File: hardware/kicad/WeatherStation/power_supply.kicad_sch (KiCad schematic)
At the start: 20 parts, among them J1 USB-C (GCT USB4105), J2 Solar 6V (JST-PH), J3 18650 LiPo (JST-PH), U2 TP4056, U2A DW01A, U3 AMS1117-3.3

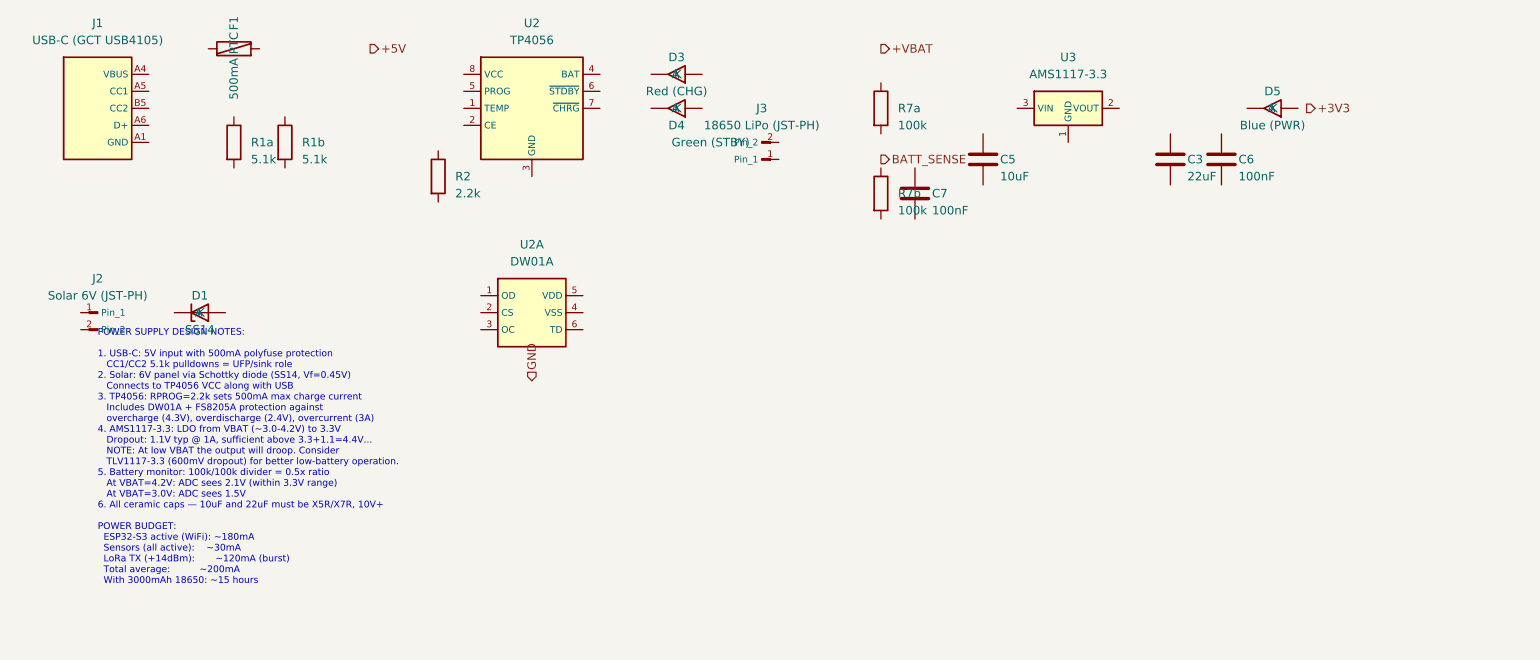
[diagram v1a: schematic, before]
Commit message: Fix 4: power_supply.kicad_sch — fix AMS1117 cap note, add VBAT cap, fix battery label, update power budget
Agent-Logs-Url: https://github.com/ppusapati/weather/sessions/bf78e071-0670-4802-a032-1f4282b37237

Co-authored-by: ppusapati <5749576+ppusapati@users.noreply.github.com>
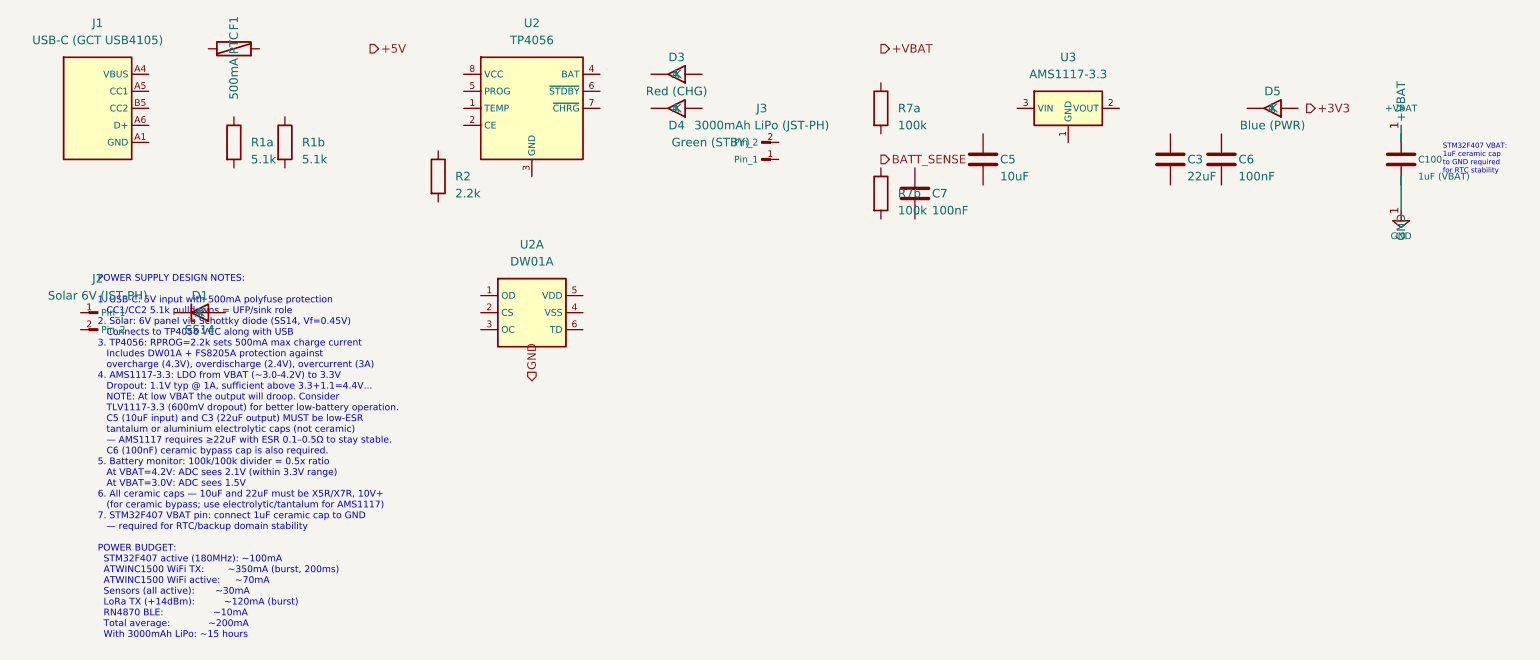
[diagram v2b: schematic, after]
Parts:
- added C100: 1uF (VBAT), symbol Device:C
- J3: value 18650 LiPo (JST-PH) -> 3000mAh LiPo (JST-PH)
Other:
- note added: "STM32F407 VBAT: 1uF ceramic cap to GND required for RTC stability"
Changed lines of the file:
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@@
     (in_bom yes) (on_board yes) (dnp no)
     (property "Reference" "J3" (at 134.62 55.88 0) (effects (font (size 1.27 1.27))))
-    (property "Value" "18650 LiPo (JST-PH)" (at 134.62 58.42 0) (effects (font (size 1.27 1.27))))
+    (property "Value" "3000mAh LiPo (JST-PH)" (at 134.62 58.42 0) (effects (font (size 1.27 1.27))))
   )
   (symbol (lib_id "Device:LED") (at 121.92 50.8 0) (unit 1)
@@
     (property "Value" "Blue (PWR)" (at 210.82 58.42 0) (effects (font (size 1.27 1.27))))
   )
+  (symbol (lib_id "Device:C") (at 230 63.5 0) (unit 1)
+    (in_bom yes) (on_board yes) (dnp no)
+    (property "Reference" "C100" (at 232.54 63.5 0) (effects (font (size 1.0 1.0)) (justify left)))
+    (property "Value" "1uF (VBAT)" (at 232.54 66.04 0) (effects (font (size 1.0 1.0)) (justify left)))
+  )
+  (symbol (lib_id "power:+VBAT") (at 230 58.42 0) (unit 1)
+    (in_bom yes) (on_board yes) (dnp no)
+    (property "Reference" "#PWR20" (at 230 62.23 0) (effects (font (size 1.0 1.0)) hide))
+    (property "Value" "+VBAT" (at 230 55.88 0) (effects (font (size 1.0 1.0))))
+    (pin "1" (uuid "20000010-0002-p1"))
+  )
+  (symbol (lib_id "power:GND") (at 230 71.12 0) (unit 1)
+    (in_bom yes) (on_board yes) (dnp no)
+    (property "Reference" "#PWR21" (at 230 77.47 0) (effects (font (size 1.0 1.0)) hide))
+    (property "Value" "GND" (at 230 74.93 0) (effects (font (size 1.0 1.0))))
+    (pin "1" (uuid "20000010-0003-p1"))
+  )
+  (text "STM32F407 VBAT:\n1uF ceramic cap\nto GND required\nfor RTC stability"
+    (at 236.22 63.5 0) (effects (font (size 0.762 0.762)) (justify left))
+  )
+  (wire (pts (xy 230 58.42) (xy 230 60.96))
+    (stroke (width 0) (type default))
+    (uuid "fix-w-vbat-top")
+  )
+  (wire (pts (xy 230 66.04) (xy 230 71.12))
+    (stroke (width 0) (type default))
+    (uuid "fix-w-vbat-bot")
+  )
   (hierarchical_label "+5V" (shape output) (at 76.2 46.99 0) (effects (font (size 1.27 1.27)) (justify left))
   )
@@
   (hierarchical_label "GND" (shape input) (at 100.33 96.52 270) (effects (font (size 1.27 1.27)) (justify left))
   )
-  (text "POWER SUPPLY DESIGN NOTES:\n\n1. USB-C: 5V input with 500mA polyfuse protection\n   CC1/CC2 5.1k pulldowns = UFP/sink role\n2. Solar: 6V panel via Schottky diode (SS14, Vf=0.45V)\n   Connects to TP4056 VCC along with USB\n3. TP4056: RPROG=2.2k sets 500mA max charge current\n   Includes DW01A + FS8205A protection against\n   overcharge (4.3V), overdischarge (2.4V), overcurrent (3A)\n4. AMS1117-3.3: LDO from VBAT (~3.0-4.2V) to 3.3V\n   Dropout: 1.1V typ @ 1A, sufficient above 3.3+1.1=4.4V...\n   NOTE: At low VBAT the output will droop. Consider\n   TLV1117-3.3 (600mV dropout) for better low-battery operation.\n5. Battery monitor: 100k/100k divider = 0.5x ratio\n   At VBAT=4.2V: ADC sees 2.1V (within 3.3V range)\n   At VBAT=3.0V: ADC sees 1.5V\n6. All ceramic caps — 10uF and 22uF must be X5R/X7R, 10V+\n\nPOWER BUDGET:\n  ESP32-S3 active (WiFi): ~180mA\n  Sensors (all active):    ~30mA\n  LoRa TX (+14dBm):       ~120mA (burst)\n  Total average:          ~200mA\n  With 3000mAh 18650: ~15 hours"
+  (text "POWER SUPPLY DESIGN NOTES:\n\n1. USB-C: 5V input with 500mA polyfuse protection\n   CC1/CC2 5.1k pulldowns = UFP/sink role\n2. Solar: 6V panel via Schottky diode (SS14, Vf=0.45V)\n   Connects to TP4056 VCC along with USB\n3. TP4056: RPROG=2.2k sets 500mA max charge current\n   Includes DW01A + FS8205A protection against\n   overcharge (4.3V), overdischarge (2.4V), overcurrent (3A)\n4. AMS1117-3.3: LDO from VBAT (~3.0-4.2V) to 3.3V\n   Dropout: 1.1V typ @ 1A, sufficient above 3.3+1.1=4.4V...\n   NOTE: At low VBAT the output will droop. Consider\n   TLV1117-3.3 (600mV dropout) for better low-battery operation.\n   C5 (10uF input) and C3 (22uF output) MUST be low-ESR\n   tantalum or aluminium electrolytic caps (not ceramic)\n   — AMS1117 requires ≥22uF with ESR 0.1–0.5Ω to stay stable.\n   C6 (100nF) ceramic bypass cap is also required.\n5. Battery monitor: 100k/100k divider = 0.5x ratio\n   At VBAT=4.2V: ADC sees 2.1V (within 3.3V range)\n   At VBAT=3.0V: ADC sees 1.5V\n6. All ceramic caps — 10uF and 22uF must be X5R/X7R, 10V+\n   (for ceramic bypass; use electrolytic/tantalum for AMS1117)\n7. STM32F407 VBAT pin: connect 1uF ceramic cap to GND\n   — required for RTC/backup domain stability\n\nPOWER BUDGET:\n  STM32F407 active (180MHz): ~100mA\n  ATWINC1500 WiFi TX:        ~350mA (burst, 200ms)\n  ATWINC1500 WiFi active:     ~70mA\n  Sensors (all active):       ~30mA\n  LoRa TX (+14dBm):          ~120mA (burst)\n  RN4870 BLE:                 ~10mA\n  Total average:             ~200mA\n  With 3000mAh LiPo: ~15 hours"
     (at 35.56 107.95 0) (effects (font (size 1.0 1.0)) (justify left))
   )

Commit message: Fix review comments: clarify battery voltage spec and AMS1117 capacitor type notes
Agent-Logs-Url: https://github.com/ppusapati/weather/sessions/bf78e071-0670-4802-a032-1f4282b37237

Co-authored-by: ppusapati <5749576+ppusapati@users.noreply.github.com>
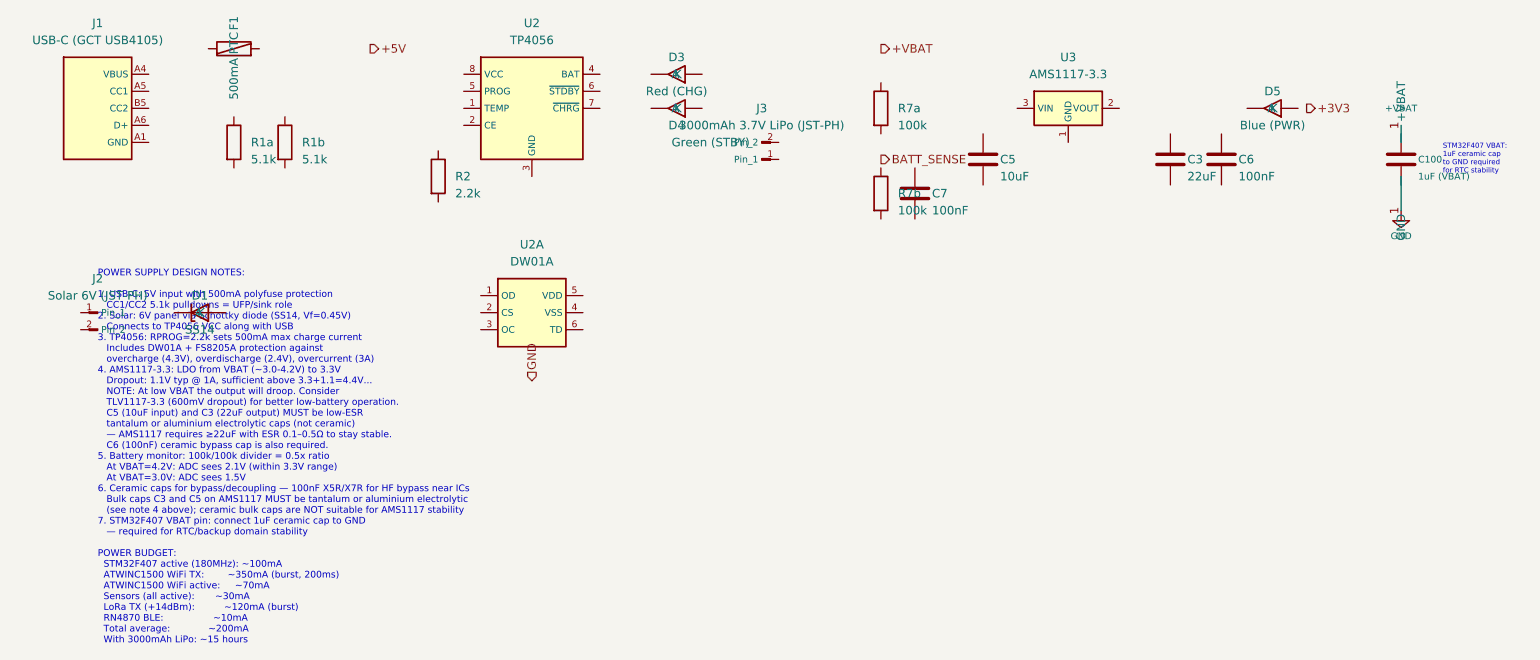
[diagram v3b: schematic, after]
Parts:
- J3: value 3000mAh LiPo (JST-PH) -> 3000mAh 3.7V LiPo (JST-PH)
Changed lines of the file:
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@@
     (in_bom yes) (on_board yes) (dnp no)
     (property "Reference" "J3" (at 134.62 55.88 0) (effects (font (size 1.27 1.27))))
-    (property "Value" "3000mAh LiPo (JST-PH)" (at 134.62 58.42 0) (effects (font (size 1.27 1.27))))
+    (property "Value" "3000mAh 3.7V LiPo (JST-PH)" (at 134.62 58.42 0) (effects (font (size 1.27 1.27))))
   )
   (symbol (lib_id "Device:LED") (at 121.92 50.8 0) (unit 1)
@@
   (hierarchical_label "GND" (shape input) (at 100.33 96.52 270) (effects (font (size 1.27 1.27)) (justify left))
   )
-  (text "POWER SUPPLY DESIGN NOTES:\n\n1. USB-C: 5V input with 500mA polyfuse protection\n   CC1/CC2 5.1k pulldowns = UFP/sink role\n2. Solar: 6V panel via Schottky diode (SS14, Vf=0.45V)\n   Connects to TP4056 VCC along with USB\n3. TP4056: RPROG=2.2k sets 500mA max charge current\n   Includes DW01A + FS8205A protection against\n   overcharge (4.3V), overdischarge (2.4V), overcurrent (3A)\n4. AMS1117-3.3: LDO from VBAT (~3.0-4.2V) to 3.3V\n   Dropout: 1.1V typ @ 1A, sufficient above 3.3+1.1=4.4V...\n   NOTE: At low VBAT the output will droop. Consider\n   TLV1117-3.3 (600mV dropout) for better low-battery operation.\n   C5 (10uF input) and C3 (22uF output) MUST be low-ESR\n   tantalum or aluminium electrolytic caps (not ceramic)\n   — AMS1117 requires ≥22uF with ESR 0.1–0.5Ω to stay stable.\n   C6 (100nF) ceramic bypass cap is also required.\n5. Battery monitor: 100k/100k divider = 0.5x ratio\n   At VBAT=4.2V: ADC sees 2.1V (within 3.3V range)\n   At VBAT=3.0V: ADC sees 1.5V\n6. All ceramic caps — 10uF and 22uF must be X5R/X7R, 10V+\n   (for ceramic bypass; use electrolytic/tantalum for AMS1117)\n7. STM32F407 VBAT pin: connect 1uF ceramic cap to GND\n   — required for RTC/backup domain stability\n\nPOWER BUDGET:\n  STM32F407 active (180MHz): ~100mA\n  ATWINC1500 WiFi TX:        ~350mA (burst, 200ms)\n  ATWINC1500 WiFi active:     ~70mA\n  Sensors (all active):       ~30mA\n  LoRa TX (+14dBm):          ~120mA (burst)\n  RN4870 BLE:                 ~10mA\n  Total average:             ~200mA\n  With 3000mAh LiPo: ~15 hours"
+  (text "POWER SUPPLY DESIGN NOTES:\n\n1. USB-C: 5V input with 500mA polyfuse protection\n   CC1/CC2 5.1k pulldowns = UFP/sink role\n2. Solar: 6V panel via Schottky diode (SS14, Vf=0.45V)\n   Connects to TP4056 VCC along with USB\n3. TP4056: RPROG=2.2k sets 500mA max charge current\n   Includes DW01A + FS8205A protection against\n   overcharge (4.3V), overdischarge (2.4V), overcurrent (3A)\n4. AMS1117-3.3: LDO from VBAT (~3.0-4.2V) to 3.3V\n   Dropout: 1.1V typ @ 1A, sufficient above 3.3+1.1=4.4V...\n   NOTE: At low VBAT the output will droop. Consider\n   TLV1117-3.3 (600mV dropout) for better low-battery operation.\n   C5 (10uF input) and C3 (22uF output) MUST be low-ESR\n   tantalum or aluminium electrolytic caps (not ceramic)\n   — AMS1117 requires ≥22uF with ESR 0.1–0.5Ω to stay stable.\n   C6 (100nF) ceramic bypass cap is also required.\n5. Battery monitor: 100k/100k divider = 0.5x ratio\n   At VBAT=4.2V: ADC sees 2.1V (within 3.3V range)\n   At VBAT=3.0V: ADC sees 1.5V\n6. Ceramic caps for bypass/decoupling — 100nF X5R/X7R for HF bypass near ICs\n   Bulk caps C3 and C5 on AMS1117 MUST be tantalum or aluminium electrolytic\n   (see note 4 above); ceramic bulk caps are NOT suitable for AMS1117 stability\n7. STM32F407 VBAT pin: connect 1uF ceramic cap to GND\n   — required for RTC/backup domain stability\n\nPOWER BUDGET:\n  STM32F407 active (180MHz): ~100mA\n  ATWINC1500 WiFi TX:        ~350mA (burst, 200ms)\n  ATWINC1500 WiFi active:     ~70mA\n  Sensors (all active):       ~30mA\n  LoRa TX (+14dBm):          ~120mA (burst)\n  RN4870 BLE:                 ~10mA\n  Total average:             ~200mA\n  With 3000mAh LiPo: ~15 hours"
     (at 35.56 107.95 0) (effects (font (size 1.0 1.0)) (justify left))
   )
